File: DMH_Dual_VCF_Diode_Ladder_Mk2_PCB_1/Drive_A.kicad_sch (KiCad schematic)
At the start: 25 parts, among them J17 Conn_01x10_PinHeader, Q1 BC548, Q2 BC548, U1 TL074

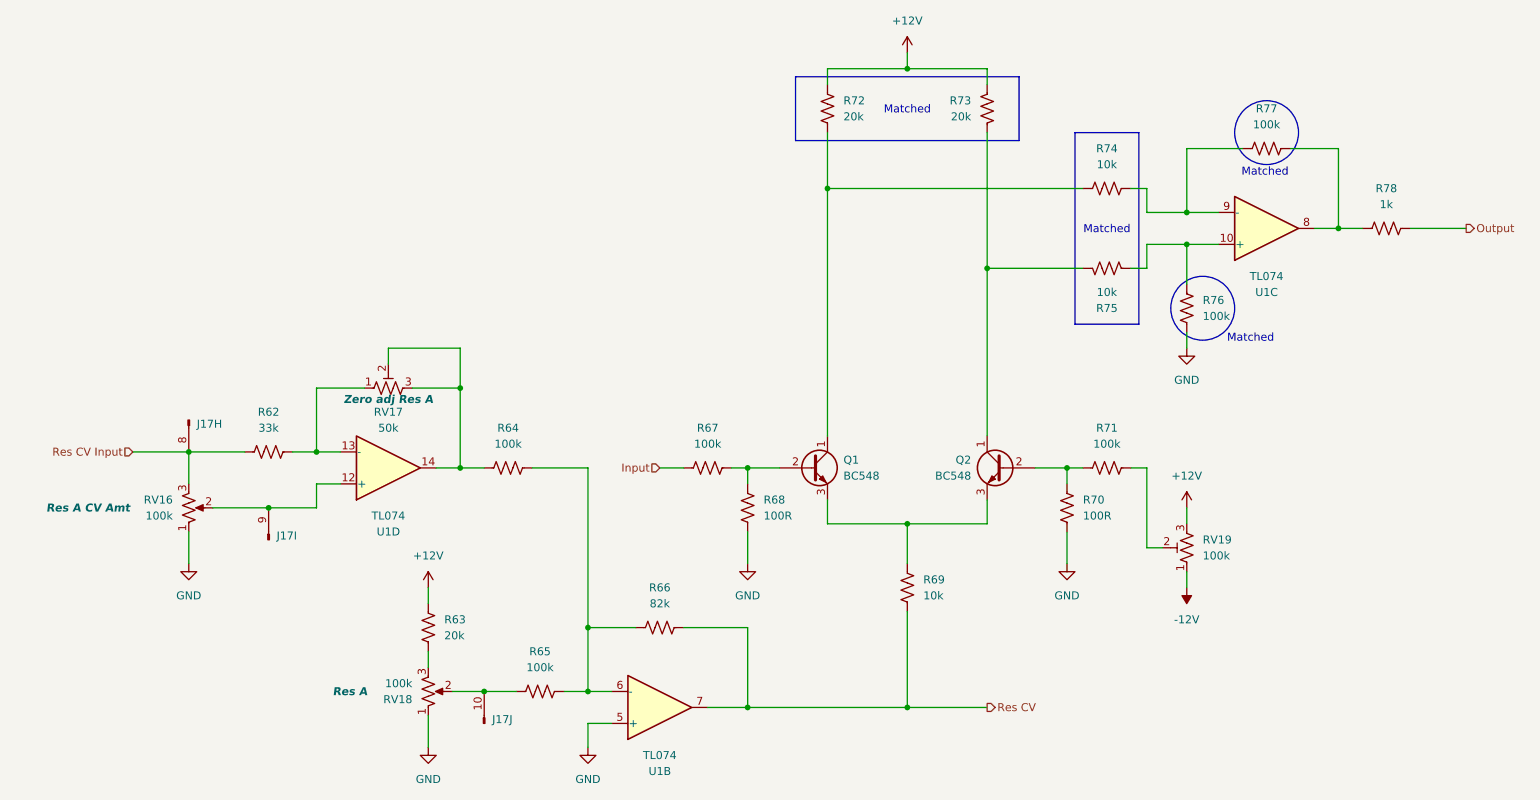
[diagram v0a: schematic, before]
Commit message: Created Drive CV circuits
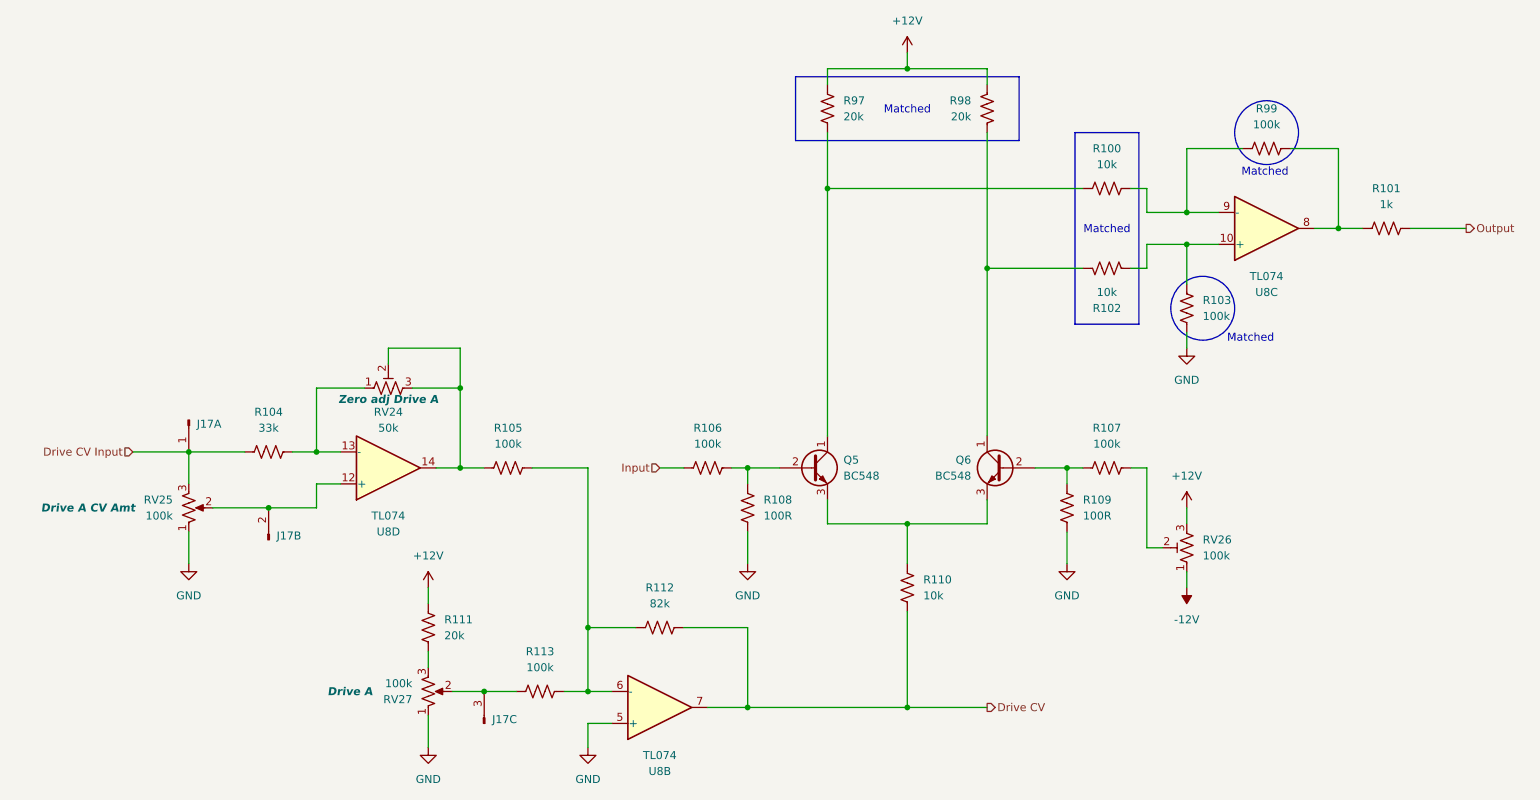
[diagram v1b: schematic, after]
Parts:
- RV24: renamed from RV17; Function Zero adj Res A -> Zero adj Drive A
- RV25: renamed from RV16; Function Res A CV Amt -> Drive A CV Amt
- RV27: renamed from RV18; Function Res A -> Drive A
- renumbered Q1 to Q5, Q2 to Q6, R74 to R100, R78 to R101, R75 to R102, R76 to R103, R62 to R104, R64 to R105, R67 to R106, R71 to R107, R68 to R108, R70 to R109, R69 to R110, R63 to R111, R66 to R112, R65 to R113, R72 to R97, R73 to R98, R77 to R99, RV19 to RV26, U1 to U8
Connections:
- net at R113.1, RV27.2: now also J17.3 (Pin_3); no longer J17.10 (Pin_10)
- net at RV25.2, U8.12 (+): now also J17.2 (Pin_2); no longer J17.9 (Pin_9)
- net Res CV renamed Drive CV
- net Res CV Input renamed Drive CV Input
- net Drive CV Input: now also J17.1 (Pin_1); no longer J17.8 (Pin_8)

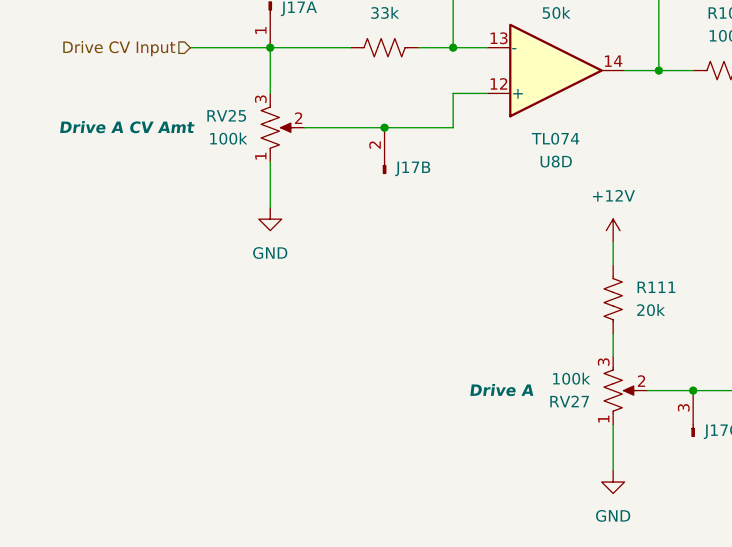
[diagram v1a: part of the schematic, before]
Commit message: Added inter-board pins to all circuits
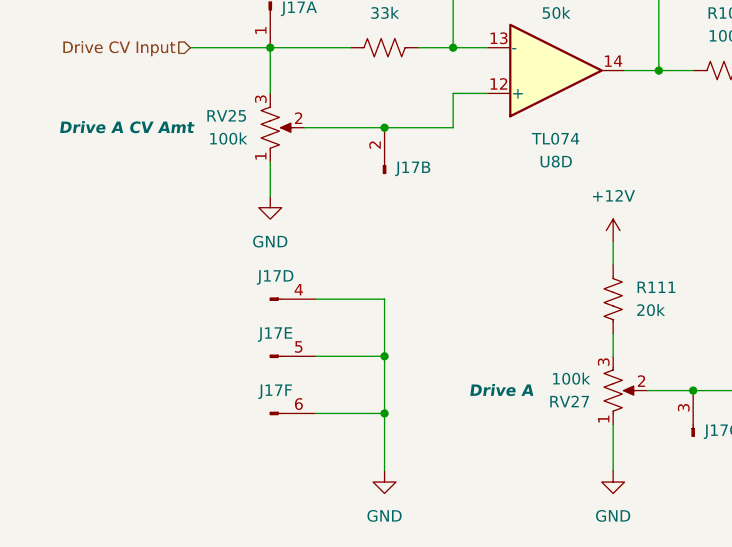
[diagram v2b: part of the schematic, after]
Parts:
- added unit 6 of J17
- added unit 5 of J17
- added unit 4 of J17
- J17: value Conn_01x10_PinHeader -> Conn_01x06_PinHeader; footprint Connector_PinHeader_2.54mm:PinHeader_1x10_P2.54mm_Vertical -> Connector_PinHeader_2.54mm:PinHeader_1x06_P2.54mm_Vertical; symbol SynthStuff:Conn_01x10_PinHeader -> SynthStuff:Conn_01x06_PinHeader
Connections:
- net GND: now also J17.4 (Pin_4), J17.5 (Pin_5), J17.6 (Pin_6)

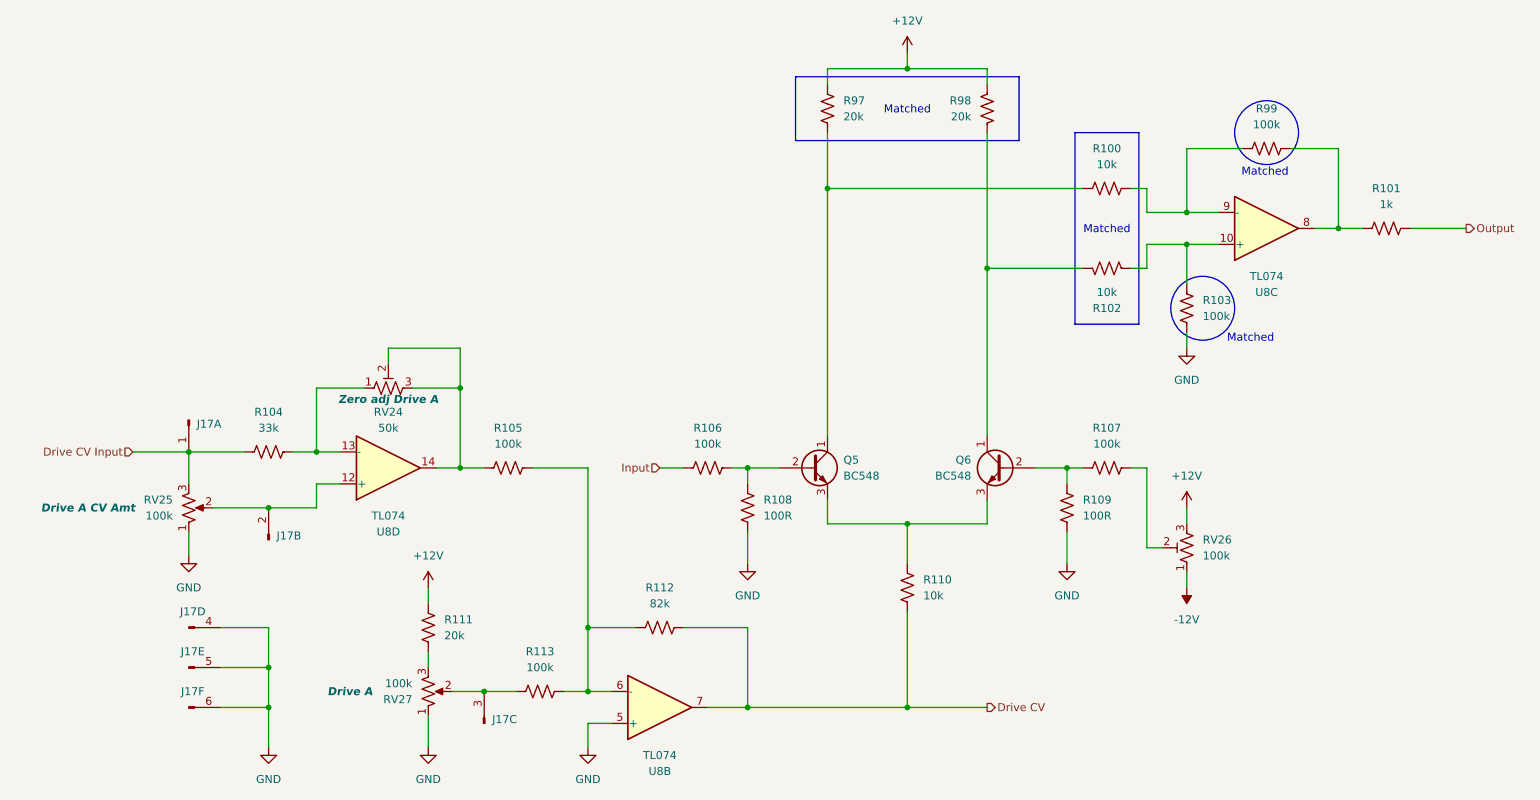
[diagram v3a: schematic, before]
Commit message: Reannotated OpAmps and cleared errors
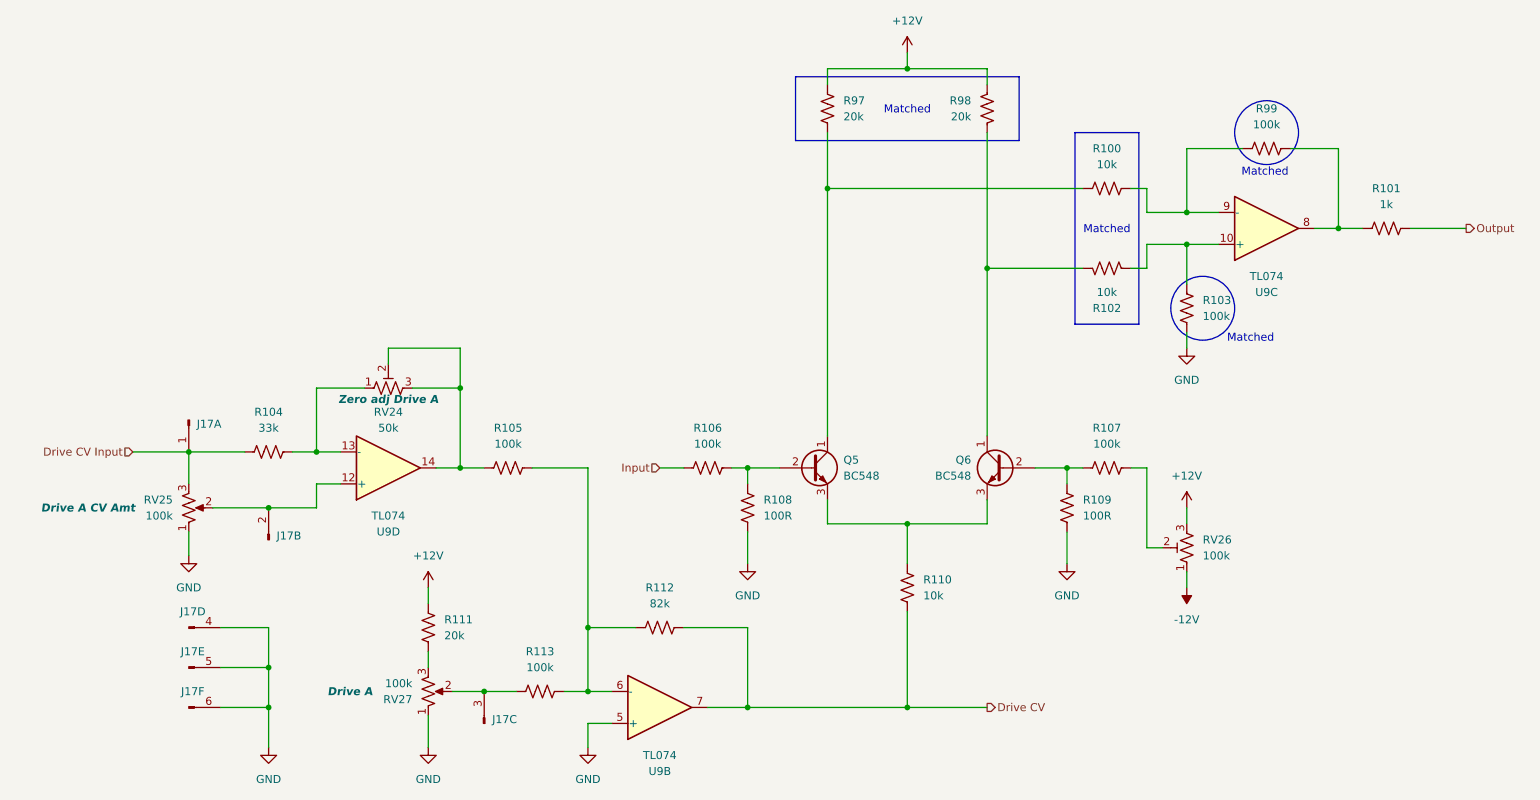
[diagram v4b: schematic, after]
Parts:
- renumbered U8 to U9
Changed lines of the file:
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@@
 		(on_board yes)
 		(dnp no)
-		(property "Reference" "U8"
+		(property "Reference" "U9"
 			(at 138.43 137.16 0)
 			(effects
@@
 			(project "DMH_Dual_VCF_Diode_Ladder_Mk2_PCB_1"
 				(path "/58f4306d-5387-4983-bb08-41a2313fd315/76f3ab41-888d-43b6-843a-2a995f9c890b"
-					(reference "U8")
+					(reference "U9")
 					(unit 2)
 				)
@@
 		(on_board yes)
 		(dnp no)
-		(property "Reference" "U8"
+		(property "Reference" "U9"
 			(at 234.95 60.96 0)
 			(effects
@@
 			(project "DMH_Dual_VCF_Diode_Ladder_Mk2_PCB_1"
 				(path "/58f4306d-5387-4983-bb08-41a2313fd315/76f3ab41-888d-43b6-843a-2a995f9c890b"
-					(reference "U8")
+					(reference "U9")
 					(unit 3)
 				)
@@
 		(on_board yes)
 		(dnp no)
-		(property "Reference" "U8"
+		(property "Reference" "U9"
 			(at 95.25 99.06 0)
 			(effects
@@
 			(project "DMH_Dual_VCF_Diode_Ladder_Mk2_PCB_1"
 				(path "/58f4306d-5387-4983-bb08-41a2313fd315/76f3ab41-888d-43b6-843a-2a995f9c890b"
-					(reference "U8")
+					(reference "U9")
 					(unit 4)
 				)
